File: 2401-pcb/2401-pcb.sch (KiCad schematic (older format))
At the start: 33 parts, among them J1 Conn_01x04_Female, Q1 SFH3710, Q2 SFH3710, SW1 SW_SPDT, U1 TLV70228_SOT23-5, U2 VL6180X, U3 LIS3DH, U4 LMV321, U5 LMV321, U6 INA126, U7 DPS422, U8 AT25SF641-SUB-T, U9 STM32G070KBT6

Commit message: Improve schematics
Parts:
- removed C6: 100nF, Capacitor_SMD:C_0603_1608Metric, symbol Device:C_Small
- added C13: 4.7uF, Capacitor_SMD:C_0805_2012Metric, symbol Device:C_Small
- added C14, C3: 100nF, Capacitor_SMD:C_0603_1608Metric, symbol Device:C_Small
- added C5: CP1_Small, Capacitor_SMD:CP_Elec_4x5.4, symbol Device:CP1_Small
- added D3: Red, LED_SMD:LED_0805_2012Metric, symbol Device:LED
- added D4: Green, LED_SMD:LED_0805_2012Metric, symbol Device:LED
- added J2: Conn_ARM_JTAG_SWD_10, Jitter_Footprints:connector_jtag_10pin_shrouded, symbol Connector:Conn_ARM_JTAG_SWD_10
- added J3: Conn_01x04_Male, Connector_PinHeader_2.54mm:PinHeader_1x04_P2.54mm_Vertical, symbol Connector:Conn_01x04_Male
- added R10, R7, R8, R9: 4k7, Resistor_SMD:R_0805_2012Metric_Pad1.15x1.40mm_HandSolder, symbol Device:R
- added R11, R12: 150, Resistor_SMD:R_0805_2012Metric_Pad1.15x1.40mm_HandSolder, symbol Device:R
- added R3, R4: 47k, Resistor_SMD:R_0805_2012Metric_Pad1.15x1.40mm_HandSolder, symbol Device:R
- C2: value 100nF -> 4.7uF; footprint Capacitor_SMD:C_0603_1608Metric -> Capacitor_SMD:C_0805_2012Metric
- gave numbers to parts that had none: 1
- renumbered C8 to C10, C3 to C11, C4 to C12, C12 to C15, C5 to C4, C11 to C6, C9 to C8, C10 to C9, R3 to R5, R4 to R6, U3 to U1, U6 to U3, U7 to U5, U5 to U6, U1 to U7, U9 to U8, U8 to U9
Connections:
- net labels added: FLASH_MISO, FLASH_MOSI, FLASH_SCLK, LED_GREEN, LED_RED, Rx, SCL, SDA, SWCLK, SWDIO, Tx, Vbatt, Vbatt_sense, accel_int1, accel_int2, distance_int, ~FLASH_CS, ~RST
- wire segments 88 -> 166
- no-connect marks 0 -> 6
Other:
- note added: ">= 1.71V\nI = 11 µA"
- note added: ">= 2.7V\nI = 1.7 mA"
- note added: "Analog Sensors"
- note added: "CS high for I2C mode"
- note added: "I2C Sensors"
- note added: "Todo: kon dit niet vinden in de datasheet, \nmaar wel bij andere chips van de 25S serie…"
- note added: "internal pull-up 30k"
- note removed: ">= 1.71V"
- note removed: "I = 1.7 mA"
- note removed: "I = 11 µA"
- moved on the sheet: BT1, C1, C10, C11, C12, C15, C2, C4, C6, C7, C8, C9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

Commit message: Schematics: finish photodiode circuit
The design calculations are in the xls file.
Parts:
- removed U4, U6: LMV321, Package_TO_SOT_SMD:SOT-23-5, symbol Amplifier_Operational:LMV321
- added C16, C18: 100nF, Capacitor_SMD:C_0603_1608Metric, symbol Device:C_Small
- added C17: 15pF, Capacitor_SMD:C_0603_1608Metric, symbol Device:C_Small
- added R13, R15: 0, Resistor_SMD:R_0805_2012Metric_Pad1.15x1.40mm_HandSolder, symbol Device:R
- added R14: 10M, Resistor_SMD:R_0805_2012Metric_Pad1.15x1.40mm_HandSolder, symbol Device:R
- added U10, U4, U6: MCP6001U, Package_TO_SOT_SMD:SOT-23-5, symbol Amplifier_Operational:MCP6001U
- BT1: value Battery_Cell -> SMTU 2450N-1-LF; footprint Battery:Battery_Panasonic_CR2450-VAN_Vertical_CircularHoles -> Jitter_Footprints:BatteryHolder_SMTU-2450N-1-LF_1x2450; Farnell (none) -> 1216356; MPN (none) -> SMTU 2450N-1-LF
- C10: value 100nF -> 15pF
- C5: value CP1_Small -> 10uF
- J1: value Conn_01x04_Female -> Load Cell; footprint Connector_JST:JST_PH_B4B-PH-SM4-TB_1x04-1MP_P2.00mm_Vertical -> Jitter_Footprints:JST_PH_S4B-PH-SM4-TB_1x04-1MP_P2.00mm_Horizontal; symbol Connector:Conn_01x04_Female -> Connector_Generic_MountingPin:Conn_01x04_MountingPin
- R1, R2, R6: value R -> 10M
- R10, R9: value 4k7 -> 47k
- R5: value R -> DNI
- U3: symbol Amplifier_Instrumentation:INA126 -> 2401-pcb-rescue:INA126-Amplifier_Instrumentation
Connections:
- wire segments 166 -> 193
- no-connect marks 6 -> 8
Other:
- note added: "0.4-0.57 nA/lx\nI_dark 0.01-5nA\n23pF"
- note added: "7-9.4 nA/lx\nI_dark 1-10nA\n135pF"
- note added: "Common emitter phototransistor circuit\nphototransistor 2 is (optionally) buffered"
- note added: "Fc @10M,15p =1Khz"
- note added: "Transimpedance amplifier\n2 different diodes"
- note removed: "Common emitter phototransistor circuit"
- note removed: "Todo: pick resistor values"
- moved on the sheet: BT1, C1, C11, C12, C13, C14, C15, C2, C3, C4, C5, C6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

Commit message: PCB: routing is more or less done
The KiCAD DRC passes, but it is not checked againts the Jitter
Checklist..
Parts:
- added C19, C20, C21, C22: 100nF, Capacitor_SMD:C_0603_1608Metric, symbol Device:C_Small
- added C23: 4.7uF, Capacitor_SMD:C_0805_2012Metric, symbol Device:C_Small
- added H1, H2: MountingHole_Pad, MountingHole:MountingHole_4.5mm_Pad_Via, symbol Mechanical:MountingHole_Pad
- added R16: DNI, Resistor_SMD:R_0805_2012Metric_Pad1.15x1.40mm_HandSolder, symbol Device:R
- added RV2: 100KΩ, Potentiometer_SMD:Potentiometer_Bourns_3314J_Vertical, symbol Device:R_POT
- added TP1, TP10, TP11, TP12, TP13, TP14, TP15, TP16, TP17, TP18, TP19, TP2, TP20, TP21, TP22, TP3, TP4, TP5, TP6, TP7, TP8, TP9: DNI, TestPoint:TestPoint_THTPad_D1.0mm_Drill0.5mm, symbol Connector:TestPoint
- added U11: MCP6001U, Package_TO_SOT_SMD:SOT-23-5, symbol Amplifier_Operational:MCP6001U
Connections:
- net +2V8: now also C21.1, C23.1, RV2.3, TP3.1, U11.5 (V+)
- net GND: now also C19.2, C20.2, C21.2, C22.2, C23.2, H1.1, H2.1, R16.1, RV2.1, U11.2 (V-); no longer U3.5 (Ref)
- net LED_GREEN: now also U8.2 (PC14-OSC32_IN); no longer U8.32 (PB8)
- net SCL: now also TP5.1
- net SDA: now also TP6.1
- net Vbatt: now also C11.1, SW1.1 (A), U7.1 (IN), U7.3 (EN), TP2.1; no longer BT1.1 (+), SW1.2 (B)
- net Vbatt_sense: now also U8.17 (PB2), C19.1, TP4.1; no longer U8.15 (PB0)
- net accel_int1: now also U8.27 (PB3); no longer U8.17 (PB2)
- net accel_int2: now also U8.28 (PB4); no longer U8.27 (PB3)
- net distance_int: now also U8.32 (PB8); no longer U8.16 (PB1)
- net load_cell: now also U8.10 (PA3), TP13.1; no longer U8.11 (PA4)
- net load_cell_out+: now also J1.3 (Pin_3), TP8.1; no longer J1.2 (Pin_2)
- net load_cell_out-: now also J1.2 (Pin_2), TP7.1; no longer J1.3 (Pin_3)
- net photo_diode_1: now also U8.11 (PA4), TP16.1; no longer U8.9 (PA2)
- net photo_diode_2: now also U8.9 (PA2), TP19.1; no longer U8.10 (PA3)
- net photo_transistor_1: now also U8.8 (PA1), TP20.1; no longer U8.7 (PA0)
- net photo_transistor_2: now also U8.7 (PA0), TP22.1; no longer U8.8 (PA1)
- net D2_V-: now reaches C17.2, D2.1 (K), R14.2, U10.3 (-)
- net D2_V-: now also TP17.1
- net D2_V+: now reaches D2.2 (A), R15.2, U10.1 (+)
- net D2_V+: now also TP18.1
- net at Q2.1 (C), R2.2, R5.2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: now also TP21.1
- net at U3.1 (Rg): now also RV1.3, TP9.1; no longer RV1.1
- net at RV1.2, U3.8 (Rg): now also TP10.1
- net D1_V+: now reaches D1.2 (A), R13.2, U6.1 (+)
- net D1_V+: now also TP15.1
- net D1_V-: now reaches C10.2, D1.1 (K), R6.2, U6.3 (-)
- net D1_V-: now also TP14.1
- new net: BT1.1 (+), SW1.2 (B), TP1.1
- new net: C22.1, RV2.2, TP11.1, U11.1 (+)
- new net load_cell_ref: C20.1, R16.2, TP12.1, U11.3 (-), U11.4, U3.5 (Ref)
- no-connect marks 8 -> 16
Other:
- note added: "(EN)"
- note added: "80.4Ω => gain = 1000 (gain = 5 + 80k/Rg)\n\nAssume load cell TAL221 with rated output 0.6 mv/V\nV = 2.8 ; gain=1000 -> 0.6*2.8=1.68V full scale"
- note added: "Load cell"
- note added: "Offset trim (optional)\n\nAdds offset to load cell output signal,\ntradeoff between inamp linearity and available gain.\nNote: inamp datasheet hints the\noutput is not rail-rail.."
- note removed: "80.4Ω => gain = 1000\n\nAssume load cell TAL221 with rated output 0.6 mv/V\nV = 2.8 so ideal gain would be 1666"
- note removed: "Load cell connector"
- note removed: "Todo: kon dit niet vinden in de datasheet, \nmaar wel bij andere chips van de 25S serie…"
- moved on the sheet: C10, C15, C16, C17, C18, C6, D1, D4, J1, R11, R12, R13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

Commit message: Schematics: reorder to similar layout as PCB
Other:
- note added: ">= 1.8V\nI = 0.1 mA (x3)"
- note added: ">= 2.7V\nI = 0.28 mA"
- note added: "Load cell (bridge amplifier)"
- note added: "Microcontroller"
- note removed: "Load cell"
- moved on the sheet: BT1, C1, C10, C11, C12, C13, C14, C15, C16, C17, C18, C19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

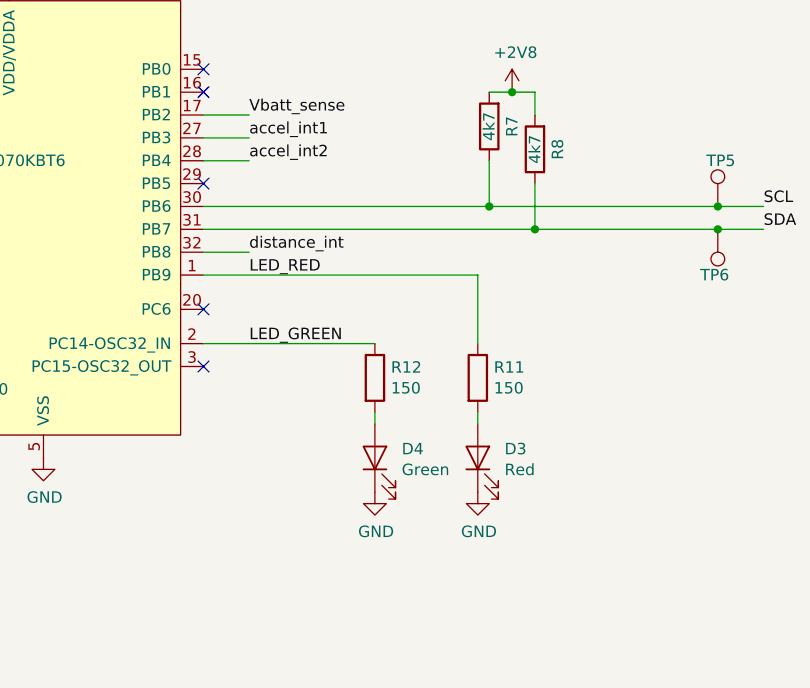
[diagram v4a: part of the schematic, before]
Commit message: Schematics: remap LED pins: PC13-15 are low-current only
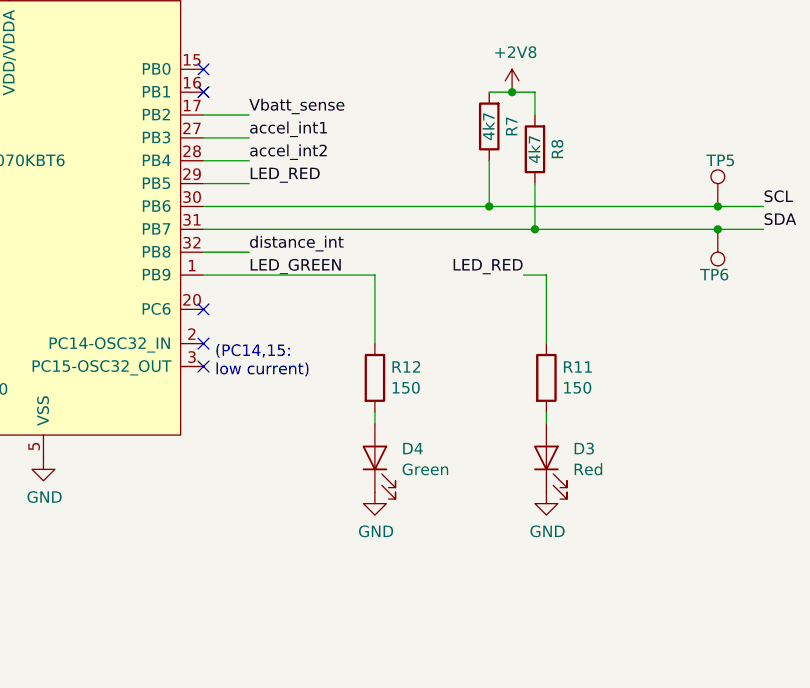
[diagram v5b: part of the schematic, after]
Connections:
- net LED_GREEN: now also U8.1 (PB9); no longer U8.2 (PC14-OSC32_IN)
- net LED_RED: now also U8.29 (PB5); no longer U8.1 (PB9)
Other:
- note added: "(PC14,15:\nlow current)"
- moved on the sheet: D3, R11
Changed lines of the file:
@@
 L Device:LED D3
 U 1 1 5E3667EE
-P 10100 10150
-F 0 "D3" V 10139 10033 50  0000 R CNN
-F 1 "Red" V 10048 10033 50  0000 R CNN
-F 2 "LED_SMD:LED_0805_2012Metric" H 10100 10150 50  0001 C CNN
-F 3 "http://www.farnell.com/datasheets/2045993.pdf" H 10100 10150 50  0001 C CNN
-F 4 "KPT-2012EC" V 10100 10150 50  0001 C CNN "MPN"
-F 5 "2099236" V 10100 10150 50  0001 C CNN "Farnell"
-	1    10100 10150
+P 10400 10150
+F 0 "D3" V 10439 10033 50  0000 R CNN
+F 1 "Red" V 10348 10033 50  0000 R CNN
+F 2 "LED_SMD:LED_0805_2012Metric" H 10400 10150 50  0001 C CNN
+F 3 "http://www.farnell.com/datasheets/2045993.pdf" H 10400 10150 50  0001 C CNN
+F 4 "KPT-2012EC" V 10400 10150 50  0001 C CNN "MPN"
+F 5 "2099236" V 10400 10150 50  0001 C CNN "Farnell"
+	1    10400 10150
 	0    -1   -1   0
 $EndComp
@@
 L Device:R R11
 U 1 1 5E36C26D
-P 10100 9800
-F 0 "R11" H 10170 9846 50  0000 L CNN
-F 1 "150" H 10170 9755 50  0000 L CNN
-F 2 "Resistor_SMD:R_0805_2012Metric_Pad1.15x1.40mm_HandSolder" V 10030 9800 50  0001 C CNN
-F 3 "~" H 10100 9800 50  0001 C CNN
-	1    10100 9800
+P 10400 9800
+F 0 "R11" H 10470 9846 50  0000 L CNN
+F 1 "150" H 10470 9755 50  0000 L CNN
+F 2 "Resistor_SMD:R_0805_2012Metric_Pad1.15x1.40mm_HandSolder" V 10330 9800 50  0001 C CNN
+F 3 "~" H 10400 9800 50  0001 C CNN
+	1    10400 9800
 	1    0    0    -1
 $EndComp
@@
 $EndComp
 Wire Wire Line
-	10100 9950 10100 10000
+	10400 9950 10400 10000
 Wire Wire Line
 	9650 9950 9650 10000
@@
 L power:GND #PWR056
 U 1 1 5E3772BB
-P 10100 10300
-F 0 "#PWR056" H 10100 10050 50  0001 C CNN
-F 1 "GND" H 10105 10127 50  0000 C CNN
-F 2 "" H 10100 10300 50  0001 C CNN
-F 3 "" H 10100 10300 50  0001 C CNN
-	1    10100 10300
+P 10400 10300
+F 0 "#PWR056" H 10400 10050 50  0001 C CNN
+F 1 "GND" H 10405 10127 50  0000 C CNN
+F 2 "" H 10400 10300 50  0001 C CNN
+F 3 "" H 10400 10300 50  0001 C CNN
+	1    10400 10300
 	1    0    0    -1
 $EndComp
@@
 $EndComp
 Wire Wire Line
-	8900 9350 10100 9350
-Wire Wire Line
-	10100 9350 10100 9650
+	10400 9350 10400 9650
+Text Label 10300 9350 2    50   ~ 0
+LED_RED
 Text Label 9100 9350 0    50   ~ 0
-LED_RED
-Text Label 9100 9650 0    50   ~ 0
 LED_GREEN
 Text Label 10350 2500 0    50   ~ 0
@@
 	2450 7500 2650 7500
 Wire Wire Line
-	9650 9650 8900 9650
+	9650 9350 8900 9350
 Wire Wire Line
 	5450 9850 7200 9850
@@
 NoConn ~ 8900 8450
 NoConn ~ 8900 8550
-NoConn ~ 8900 8950
+NoConn ~ 8900 9650
 NoConn ~ 8900 9500
 NoConn ~ 8900 9750
@@
 Text Notes 850  1100 0    50   ~ 0
 >= 2.7V\nI = 0.28 mA
+Text Label 9100 8950 0    50   ~ 0
+LED_RED
+Wire Wire Line
+	9100 8950 8900 8950
+Wire Wire Line
+	10400 9350 10300 9350
+Wire Wire Line
+	9650 9350 9650 9650
+Text Notes 8950 9800 0    50   ~ 0
+(PC14,15:\nlow current)
 $EndSCHEMATC

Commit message: PCB: schematics & layout complete [Checklist PASS]
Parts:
- added LOGO1, LOGO3: LOGO, Jitter_Logos:Jitter, symbol Jitter_Components:LOGO
- added LOGO2, LOGO4: LOGO, Jitter_Logos:Symbol_Jitter-Icon_CopperAndSilkScreenTop, symbol Jitter_Components:LOGO
- added MB1, MB2, MB3, MB4: Mousebite, Jitter_Footprints:MouseBite_3.5mmx2.2mm_breakaway, symbol Mechanical:MountingHole
- added TH1, TH2, TH3, TH4: ToolingHole, Jitter_Footprints:Tooling_hole_4mm_4.04mm_paste, symbol Mechanical:MountingHole
- TP14, TP17: footprint TestPoint:TestPoint_THTPad_D1.0mm_Drill0.5mm -> TestPoint:TestPoint_Pad_D1.0mm
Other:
- note added: "Note: guard ring\naround sensitive\ninput"
- moved on the sheet: R14, R6, TP14, TP15, TP17, TP18

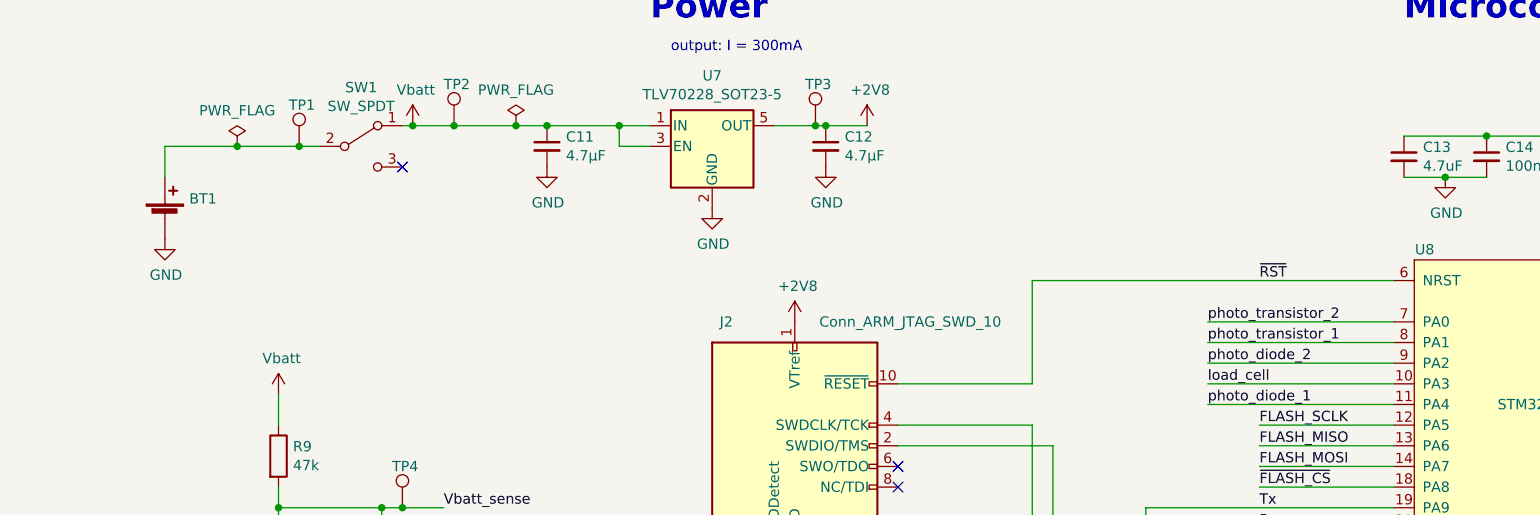
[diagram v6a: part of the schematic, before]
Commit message: PCB/Schematic bugfix: add NRST capacitor, update air pressure symbol
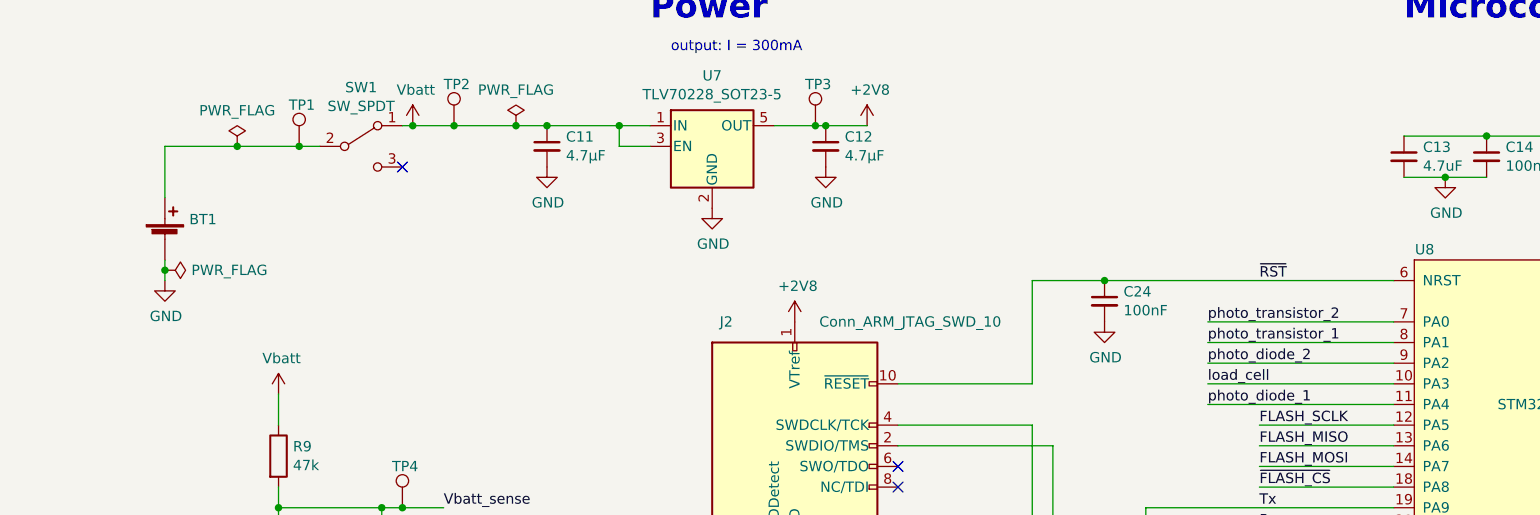
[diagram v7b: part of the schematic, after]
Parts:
- added C24: 100nF, Capacitor_SMD:C_0603_1608Metric, symbol Device:C_Small
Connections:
- net GND: now also C24.2
- net ~RST: now also C24.1
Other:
- moved on the sheet: BT1

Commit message: Schematics: don't reference rescue library
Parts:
- U5: symbol 2401-pcb-rescue:DPS422-Jitter_Components -> Jitter_Components:DPS422
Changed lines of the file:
@@
 Connection ~ 14450 5550
 $Comp
-L 2401-pcb-rescue:DPS422-Jitter_Components U5
+L Jitter_Components:DPS422 U5
 U 1 1 5E20A247
-P 14600 5050
-F 0 "U5" H 14250 5500 50  0000 L CNN
-F 1 "DPS422" H 14550 5250 50  0000 L CNN
-F 2 "Package_LGA:Bosch_LGA-8_2x2.5mm_P0.65mm_ClockwisePinNumbering" H 14600 5900 118 0001 C CNN
-F 3 "https://www.infineon.com/dgdl/Infineon-DPS422-DS-v01_03-EN.pdf?fileId=5546d46264fee02f01650249502c1ddf" H 14600 5900 118 0001 C CNN
-	1    14600 5050
+P 14550 5050
+F 0 "U5" H 14600 5700 50  0000 L CNN
+F 1 "DPS422" H 14600 5600 50  0000 L CNN
+F 2 "Package_LGA:Bosch_LGA-8_2x2.5mm_P0.65mm_ClockwisePinNumbering" H 14550 5900 118 0001 C CNN
+F 3 "https://www.infineon.com/dgdl/Infineon-DPS422-DS-v01_03-EN.pdf?fileId=5546d46264fee02f01650249502c1ddf" H 14550 5900 118 0001 C CNN
+	1    14550 5050
 	1    0    0    -1
 $EndComp
